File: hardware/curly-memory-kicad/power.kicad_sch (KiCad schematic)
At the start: 19 parts

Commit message: schematic updated with component fields on more components
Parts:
- C? (x5): value C -> 1uF; footprint (none) -> Capacitor_SMD:C_0805_2012Metric_Pad1.18x1.45mm_HandSolder
- C? (x5): value C -> 100nF; footprint (none) -> Capacitor_SMD:C_0805_2012Metric_Pad1.18x1.45mm_HandSolder
- C? (x2): footprint (none) -> Capacitor_SMD:C_0805_2012Metric_Pad1.18x1.45mm_HandSolder
- D? (x2): footprint (none) -> Diode_SMD:D_SMA-SMB_Universal_Handsoldering
- J?: footprint (none) -> Connector_IDC:IDC-Header_2x05_P2.54mm_Vertical
- R? (x2): footprint (none) -> Resistor_SMD:R_0805_2012Metric_Pad1.20x1.40mm_HandSolder
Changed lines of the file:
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@@
       (effects (font (size 1.27 1.27)) (justify left))
     )
-    (property "Value" "C" (id 1) (at 109.601 94.488 0)
-      (effects (font (size 1.27 1.27)) (justify left))
-    )
-    (property "Footprint" "" (id 2) (at 107.6452 97.155 0)
+    (property "Value" "1uF" (id 1) (at 109.601 94.488 0)
+      (effects (font (size 1.27 1.27)) (justify left))
+    )
+    (property "Footprint" "Capacitor_SMD:C_0805_2012Metric_Pad1.18x1.45mm_HandSolder" (id 2) (at 107.6452 97.155 0)
       (effects (font (size 1.27 1.27)) hide)
     )
@@
       (effects (font (size 1.27 1.27)) (justify left))
     )
-    (property "Footprint" "" (id 2) (at 74.422 142.875 90)
+    (property "Footprint" "Resistor_SMD:R_0805_2012Metric_Pad1.20x1.40mm_HandSolder" (id 2) (at 74.422 142.875 90)
       (effects (font (size 1.27 1.27)) hide)
     )
@@
       (effects (font (size 1.27 1.27)) (justify left))
     )
-    (property "Value" "C" (id 1) (at 118.491 94.488 0)
-      (effects (font (size 1.27 1.27)) (justify left))
-    )
-    (property "Footprint" "" (id 2) (at 116.5352 97.155 0)
+    (property "Value" "100nF" (id 1) (at 118.491 94.488 0)
+      (effects (font (size 1.27 1.27)) (justify left))
+    )
+    (property "Footprint" "Capacitor_SMD:C_0805_2012Metric_Pad1.18x1.45mm_HandSolder" (id 2) (at 116.5352 97.155 0)
       (effects (font (size 1.27 1.27)) hide)
     )
@@
       (effects (font (size 1.27 1.27)) (justify left))
     )
-    (property "Value" "C" (id 1) (at 73.406 47.498 0)
-      (effects (font (size 1.27 1.27)) (justify left))
-    )
-    (property "Footprint" "" (id 2) (at 71.4502 50.165 0)
+    (property "Value" "1uF" (id 1) (at 73.406 47.498 0)
+      (effects (font (size 1.27 1.27)) (justify left))
+    )
+    (property "Footprint" "Capacitor_SMD:C_0805_2012Metric_Pad1.18x1.45mm_HandSolder" (id 2) (at 71.4502 50.165 0)
       (effects (font (size 1.27 1.27)) hide)
     )
@@
     (property "Reference" "J?" (id 0) (at 40.64 35.56 0))
     (property "Value" "Conn_02x05_Odd_Even" (id 1) (at 41.91 33.655 0))
-    (property "Footprint" "" (id 2) (at 41.91 46.355 0)
+    (property "Footprint" "Connector_IDC:IDC-Header_2x05_P2.54mm_Vertical" (id 2) (at 41.91 46.355 0)
       (effects (font (size 1.27 1.27)) hide)
     )
@@
       (effects (font (size 1.27 1.27)) (justify left))
     )
-    (property "Value" "C" (id 1) (at 82.296 47.498 0)
-      (effects (font (size 1.27 1.27)) (justify left))
-    )
-    (property "Footprint" "" (id 2) (at 80.3402 50.165 0)
+    (property "Value" "100nF" (id 1) (at 82.296 47.498 0)
+      (effects (font (size 1.27 1.27)) (justify left))
+    )
+    (property "Footprint" "Capacitor_SMD:C_0805_2012Metric_Pad1.18x1.45mm_HandSolder" (id 2) (at 80.3402 50.165 0)
       (effects (font (size 1.27 1.27)) hide)
     )
@@
       (effects (font (size 1.27 1.27)) (justify left))
     )
-    (property "Value" "C" (id 1) (at 81.661 94.488 0)
-      (effects (font (size 1.27 1.27)) (justify left))
-    )
-    (property "Footprint" "" (id 2) (at 79.7052 97.155 0)
+    (property "Value" "100nF" (id 1) (at 81.661 94.488 0)
+      (effects (font (size 1.27 1.27)) (justify left))
+    )
+    (property "Footprint" "Capacitor_SMD:C_0805_2012Metric_Pad1.18x1.45mm_HandSolder" (id 2) (at 79.7052 97.155 0)
       (effects (font (size 1.27 1.27)) hide)
     )
@@
       (effects (font (size 1.27 1.27)) (justify left))
     )
-    (property "Footprint" "" (id 2) (at 65.7352 141.605 0)
+    (property "Footprint" "Capacitor_SMD:C_0805_2012Metric_Pad1.18x1.45mm_HandSolder" (id 2) (at 65.7352 141.605 0)
       (effects (font (size 1.27 1.27)) hide)
     )
@@
       (effects (font (size 1.27 1.27)) (justify left))
     )
-    (property "Value" "C" (id 1) (at 72.771 94.488 0)
-      (effects (font (size 1.27 1.27)) (justify left))
-    )
-    (property "Footprint" "" (id 2) (at 70.8152 97.155 0)
+    (property "Value" "1uF" (id 1) (at 72.771 94.488 0)
+      (effects (font (size 1.27 1.27)) (justify left))
+    )
+    (property "Footprint" "Capacitor_SMD:C_0805_2012Metric_Pad1.18x1.45mm_HandSolder" (id 2) (at 70.8152 97.155 0)
       (effects (font (size 1.27 1.27)) hide)
     )
@@
     (property "Reference" "D?" (id 0) (at 55.88 35.7632 0))
     (property "Value" "D" (id 1) (at 55.88 38.0746 0))
-    (property "Footprint" "" (id 2) (at 55.88 41.275 0)
+    (property "Footprint" "Diode_SMD:D_SMA-SMB_Universal_Handsoldering" (id 2) (at 55.88 41.275 0)
       (effects (font (size 1.27 1.27)) hide)
     )
@@
       (effects (font (size 1.27 1.27)) (justify left))
     )
-    (property "Value" "C" (id 1) (at 82.296 65.278 0)
-      (effects (font (size 1.27 1.27)) (justify left))
-    )
-    (property "Footprint" "" (id 2) (at 80.3402 67.945 0)
+    (property "Value" "100nF" (id 1) (at 82.296 65.278 0)
+      (effects (font (size 1.27 1.27)) (justify left))
+    )
+    (property "Footprint" "Capacitor_SMD:C_0805_2012Metric_Pad1.18x1.45mm_HandSolder" (id 2) (at 80.3402 67.945 0)
       (effects (font (size 1.27 1.27)) hide)
     )
@@
       (effects (font (size 1.27 1.27)) (justify left))
     )
-    (property "Value" "C" (id 1) (at 73.406 65.278 0)
-      (effects (font (size 1.27 1.27)) (justify left))
-    )
-    (property "Footprint" "" (id 2) (at 71.4502 67.945 0)
+    (property "Value" "1uF" (id 1) (at 73.406 65.278 0)
+      (effects (font (size 1.27 1.27)) (justify left))
+    )
+    (property "Footprint" "Capacitor_SMD:C_0805_2012Metric_Pad1.18x1.45mm_HandSolder" (id 2) (at 71.4502 67.945 0)
       (effects (font (size 1.27 1.27)) hide)
     )
@@
       (effects (font (size 1.27 1.27)) (justify left))
     )
-    (property "Footprint" "" (id 2) (at 88.5952 146.685 0)
+    (property "Footprint" "Capacitor_SMD:C_0805_2012Metric_Pad1.18x1.45mm_HandSolder" (id 2) (at 88.5952 146.685 0)
       (effects (font (size 1.27 1.27)) hide)
     )
@@
       (effects (font (size 1.27 1.27)) (justify left))
     )
-    (property "Value" "C" (id 1) (at 109.601 47.498 0)
-      (effects (font (size 1.27 1.27)) (justify left))
-    )
-    (property "Footprint" "" (id 2) (at 107.6452 50.165 0)
+    (property "Value" "1uF" (id 1) (at 109.601 47.498 0)
+      (effects (font (size 1.27 1.27)) (justify left))
+    )
+    (property "Footprint" "Capacitor_SMD:C_0805_2012Metric_Pad1.18x1.45mm_HandSolder" (id 2) (at 107.6452 50.165 0)
       (effects (font (size 1.27 1.27)) hide)
     )
@@
       (effects (font (size 1.27 1.27)) (justify left))
     )
-    (property "Value" "C" (id 1) (at 118.491 47.498 0)
-      (effects (font (size 1.27 1.27)) (justify left))
-    )
-    (property "Footprint" "" (id 2) (at 116.5352 50.165 0)
+    (property "Value" "100nF" (id 1) (at 118.491 47.498 0)
+      (effects (font (size 1.27 1.27)) (justify left))
+    )
+    (property "Footprint" "Capacitor_SMD:C_0805_2012Metric_Pad1.18x1.45mm_HandSolder" (id 2) (at 116.5352 50.165 0)
       (effects (font (size 1.27 1.27)) hide)
     )
@@
       (effects (font (size 1.27 1.27)) (justify left))
     )
-    (property "Footprint" "" (id 2) (at 74.422 132.715 90)
+    (property "Footprint" "Resistor_SMD:R_0805_2012Metric_Pad1.20x1.40mm_HandSolder" (id 2) (at 74.422 132.715 90)
       (effects (font (size 1.27 1.27)) hide)
     )
@@
     (property "Reference" "D?" (id 0) (at 55.88 64.135 0))
     (property "Value" "D" (id 1) (at 55.88 61.595 0))
-    (property "Footprint" "" (id 2) (at 55.88 59.055 0)
-      (effects (font (size 1.27 1.27)) hide)
-    )
+    (property "Footprint" "Diode_SMD:D_SMA-SMB_Universal_Handsoldering" (id 2) (at 55.88 59.055 0)
+      (effects (font (size 1.27 1.27)) hide)
+    )

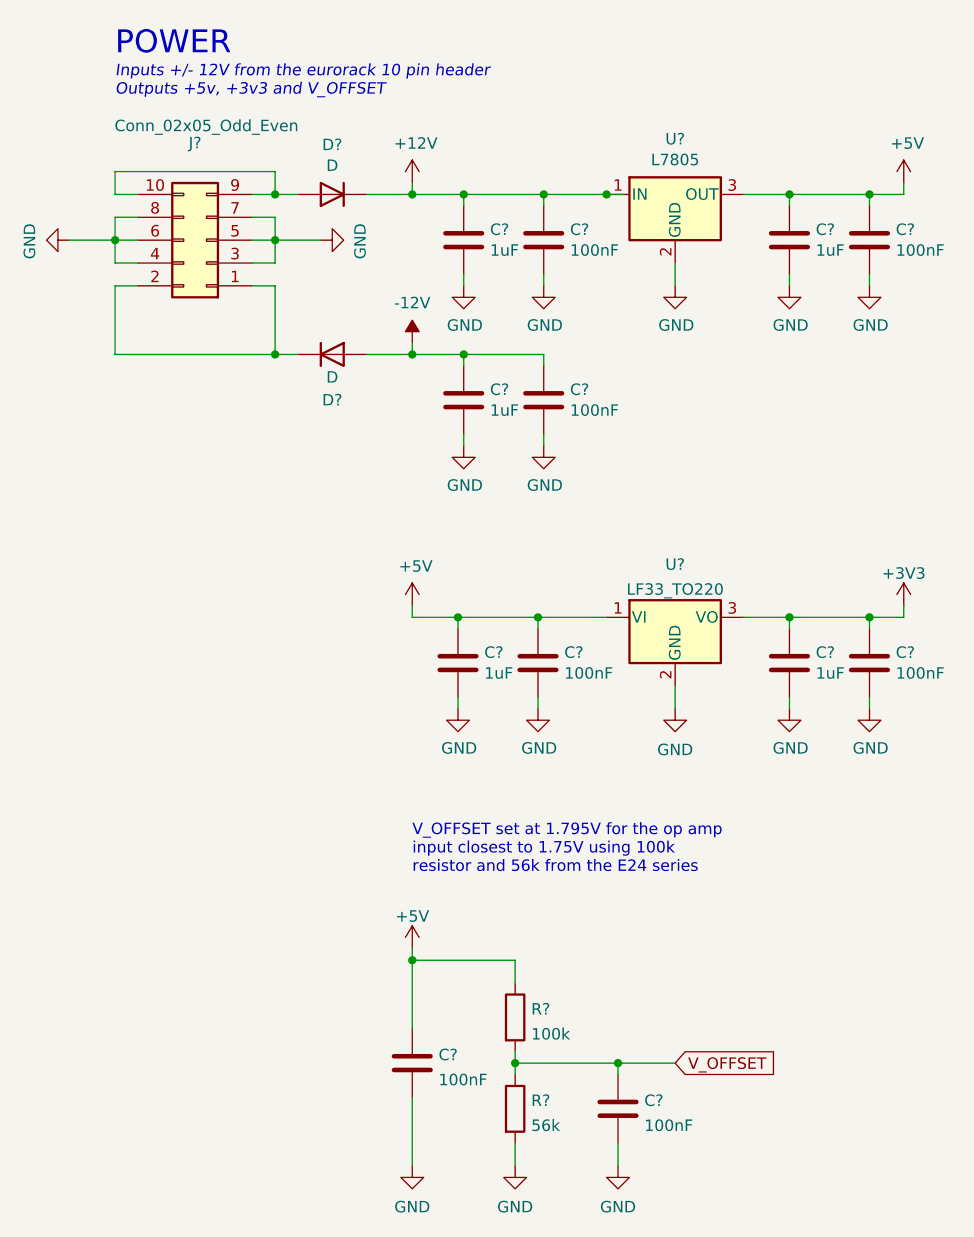
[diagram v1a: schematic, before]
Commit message: all components have part numbers
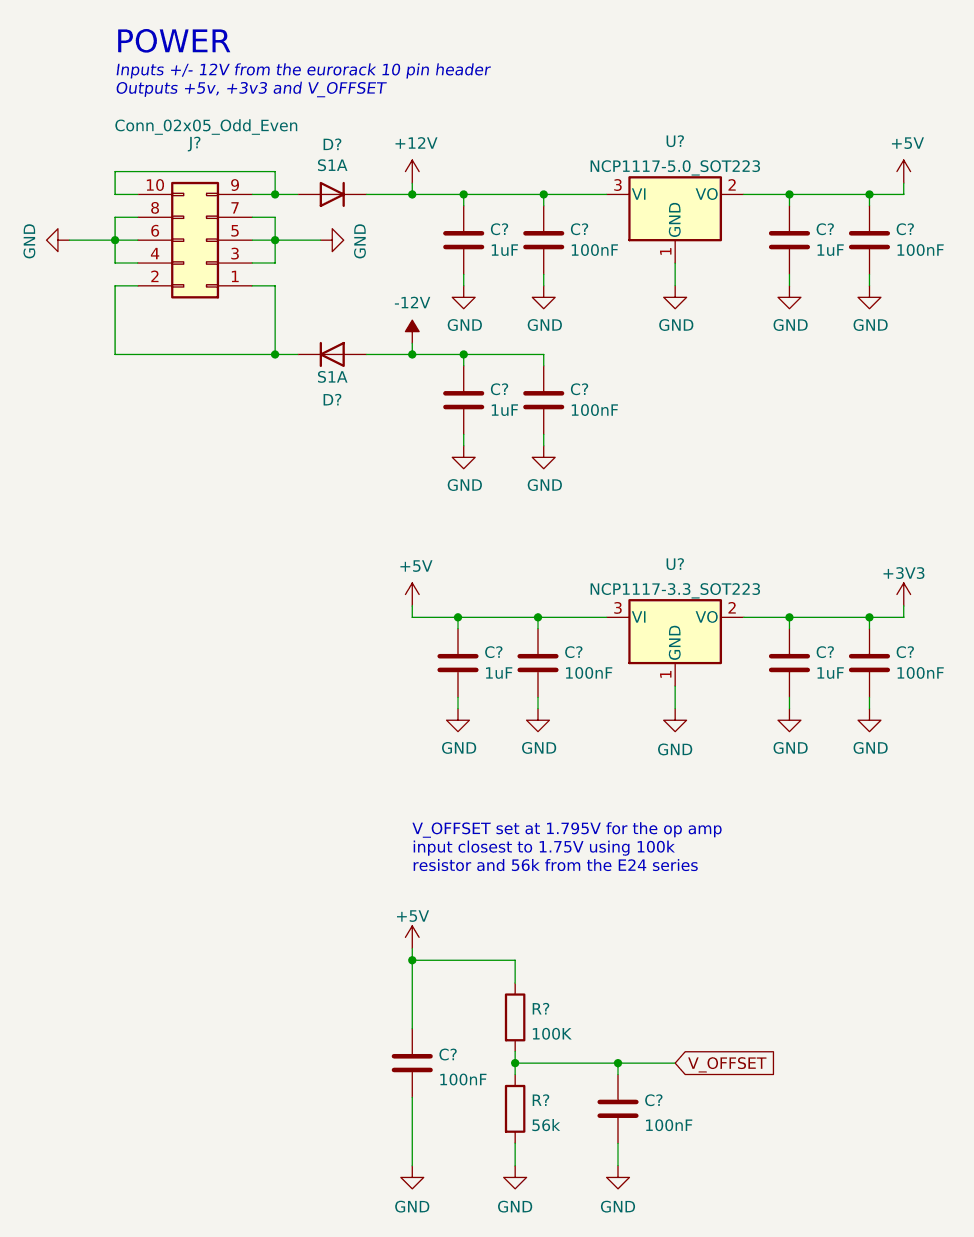
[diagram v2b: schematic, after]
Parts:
- removed U?: L7805, symbol Regulator_Linear:L7805
- removed U?: LF33_TO220, Package_TO_SOT_THT:TO-220-3_Vertical, symbol Regulator_Linear:LF33_TO220
- added U?: NCP1117-5.0_SOT223, Package_TO_SOT_SMD:SOT-223-3_TabPin2, symbol Regulator_Linear:NCP1117-5.0_SOT223
- added U?: NCP1117-3.3_SOT223, Package_TO_SOT_SMD:SOT-223-3_TabPin2, symbol Regulator_Linear:NCP1117-3.3_SOT223
- D? (x2): value D -> S1A
- R?: value 100k -> 100K
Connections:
- net +12V: now also U?.3 (VI)
- net +3V3: now also U?.2 (VO)
- net +5V: now also U?.2 (VO), U?.3 (VI)
- net GND: now also U?.1 (GND), U?.1 (GND)
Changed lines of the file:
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@@
   (junction (at 70.485 59.055) (diameter 0) (color 0 0 0 0)
   )
+  (junction (at 64.77 59.055) (diameter 0) (color 0 0 0 0)
+  )
+  (junction (at 31.75 46.355) (diameter 0) (color 0 0 0 0)
+  )
+  (junction (at 106.68 41.275) (diameter 0) (color 0 0 0 0)
+  )
+  (junction (at 70.485 41.275) (diameter 0) (color 0 0 0 0)
+  )
+  (junction (at 49.53 41.275) (diameter 0) (color 0 0 0 0)
+  )
+  (junction (at 115.57 88.265) (diameter 0) (color 0 0 0 0)
+  )
+  (junction (at 115.57 41.275) (diameter 0) (color 0 0 0 0)
+  )
+  (junction (at 106.68 88.265) (diameter 0) (color 0 0 0 0)
+  )
+  (junction (at 69.85 88.265) (diameter 0) (color 0 0 0 0)
+  )
+  (junction (at 78.74 88.265) (diameter 0) (color 0 0 0 0)
+  )
   (junction (at 79.375 41.275) (diameter 0) (color 0 0 0 0)
   )
-  (junction (at 64.77 59.055) (diameter 0) (color 0 0 0 0)
-  )
-  (junction (at 31.75 46.355) (diameter 0) (color 0 0 0 0)
-  )
-  (junction (at 106.68 41.275) (diameter 0) (color 0 0 0 0)
-  )
-  (junction (at 86.36 41.275) (diameter 0) (color 0 0 0 0)
-  )
-  (junction (at 70.485 41.275) (diameter 0) (color 0 0 0 0)
-  )
-  (junction (at 49.53 41.275) (diameter 0) (color 0 0 0 0)
-  )
-  (junction (at 115.57 88.265) (diameter 0) (color 0 0 0 0)
-  )
-  (junction (at 115.57 41.275) (diameter 0) (color 0 0 0 0)
-  )
-  (junction (at 106.68 88.265) (diameter 0) (color 0 0 0 0)
-  )
-  (junction (at 69.85 88.265) (diameter 0) (color 0 0 0 0)
-  )
-  (junction (at 78.74 88.265) (diameter 0) (color 0 0 0 0)
-  )
   (junction (at 49.53 46.355) (diameter 0) (color 0 0 0 0)
   )
@@
     (stroke (width 0) (type default) (color 0 0 0 0))
   )
-  (wire (pts (xy 86.36 41.275) (xy 88.265 41.275))
-    (stroke (width 0) (type default) (color 0 0 0 0))
-  )
   (wire (pts (xy 64.77 57.785) (xy 64.77 59.055))
     (stroke (width 0) (type default) (color 0 0 0 0))
@@
     (stroke (width 0) (type default) (color 0 0 0 0))
   )
+  (wire (pts (xy 79.375 41.275) (xy 86.36 41.275))
+    (stroke (width 0) (type default) (color 0 0 0 0))
+  )
   (wire (pts (xy 31.75 46.355) (xy 31.75 48.895))
     (stroke (width 0) (type default) (color 0 0 0 0))
   )
   (wire (pts (xy 76.2 136.525) (xy 76.2 137.795))
-    (stroke (width 0) (type default) (color 0 0 0 0))
-  )
-  (wire (pts (xy 79.375 41.275) (xy 86.36 41.275))
     (stroke (width 0) (type default) (color 0 0 0 0))
   )
@@
     (pin "2")
   )
-  (symbol (lib_id "Regulator_Linear:L7805") (at 93.98 41.275 0) (unit 1)
-    (in_bom yes) (on_board yes)
-    (property "Reference" "U?" (id 0) (at 93.98 35.1282 0))
-    (property "Value" "L7805" (id 1) (at 93.98 37.4396 0))
-    (property "Footprint" "" (id 2) (at 94.615 45.085 0)
-      (effects (font (size 1.27 1.27) italic) (justify left) hide)
-    )
-    (property "Datasheet" "http://www.st.com/content/ccc/resource/technical/document/datasheet/41/4f/b3/b0/12/d4/47/88/CD00000444.pdf/files/CD00000444.pdf/jcr:content/translations/en.CD00000444.pdf" (id 3) (at 93.98 42.545 0)
-      (effects (font (size 1.27 1.27)) hide)
-    )
-    (pin "1")
-    (pin "2")
-    (pin "3")
-  )
   (symbol (lib_id "power:+3V3") (at 119.38 86.995 0) (unit 1)
     (in_bom yes) (on_board yes) (fields_autoplaced)
@@
     (pin "1")
   )
-  (symbol (lib_id "Regulator_Linear:LF33_TO220") (at 93.98 88.265 0) (unit 1)
-    (in_bom yes) (on_board yes) (fields_autoplaced)
-    (property "Reference" "U?" (id 0) (at 93.98 82.3935 0))
-    (property "Value" "LF33_TO220" (id 1) (at 93.98 85.1686 0))
-    (property "Footprint" "Package_TO_SOT_THT:TO-220-3_Vertical" (id 2) (at 93.98 82.55 0)
-      (effects (font (size 1.27 1.27) italic) hide)
-    )
-    (property "Datasheet" "http://www.st.com/content/ccc/resource/technical/document/datasheet/c4/0e/7e/2a/be/bc/4c/bd/CD00000546.pdf/files/CD00000546.pdf/jcr:content/translations/en.CD00000546.pdf" (id 3) (at 93.98 89.535 0)
-      (effects (font (size 1.27 1.27)) hide)
-    )
-    (pin "1")
-    (pin "2")
-    (pin "3")
-  )
   (symbol (lib_id "Device:C") (at 78.74 93.345 0) (unit 1)
     (in_bom yes) (on_board yes)
@@
     (pin "1")
   )
+  (symbol (lib_id "Regulator_Linear:NCP1117-5.0_SOT223") (at 93.98 41.275 0) (unit 1)
+    (in_bom yes) (on_board yes) (fields_autoplaced)
+    (property "Reference" "U?" (id 0) (at 93.98 35.4035 0))
+    (property "Value" "NCP1117-5.0_SOT223" (id 1) (at 93.98 38.1786 0))
+    (property "Footprint" "Package_TO_SOT_SMD:SOT-223-3_TabPin2" (id 2) (at 93.98 36.195 0)
+      (effects (font (size 1.27 1.27)) hide)
+    )
+    (property "Datasheet" "http://www.onsemi.com/pub_link/Collateral/NCP1117-D.PDF" (id 3) (at 96.52 47.625 0)
+      (effects (font (size 1.27 1.27)) hide)
+    )
+    (pin "1")
+    (pin "2")
+    (pin "3")
+  )
   (symbol (lib_name "GND_16") (lib_id "power:GND") (at 87.63 149.225 0) (unit 1)
     (in_bom yes) (on_board yes) (fields_autoplaced)
@@
     (in_bom yes) (on_board yes)
     (property "Reference" "D?" (id 0) (at 55.88 35.7632 0))
-    (property "Value" "D" (id 1) (at 55.88 38.0746 0))
+    (property "Value" "S1A" (id 1) (at 55.88 38.0746 0))
     (property "Footprint" "Diode_SMD:D_SMA-SMB_Universal_Handsoldering" (id 2) (at 55.88 41.275 0)
       (effects (font (size 1.27 1.27)) hide)
@@
     (pin "1")
   )
+  (symbol (lib_id "Regulator_Linear:NCP1117-3.3_SOT223") (at 93.98 88.265 0) (unit 1)
+    (in_bom yes) (on_board yes) (fields_autoplaced)
+    (property "Reference" "U?" (id 0) (at 93.98 82.3935 0))
+    (property "Value" "NCP1117-3.3_SOT223" (id 1) (at 93.98 85.1686 0))
+    (property "Footprint" "Package_TO_SOT_SMD:SOT-223-3_TabPin2" (id 2) (at 93.98 83.185 0)
+      (effects (font (size 1.27 1.27)) hide)
+    )
+    (property "Datasheet" "http://www.onsemi.com/pub_link/Collateral/NCP1117-D.PDF" (id 3) (at 96.52 94.615 0)
+      (effects (font (size 1.27 1.27)) hide)
+    )
+    (pin "1")
+    (pin "2")
+    (pin "3")
+  )
   (symbol (lib_id "Device:C") (at 70.485 64.135 0) (unit 1)
     (in_bom yes) (on_board yes)
@@
       (effects (font (size 1.27 1.27)) (justify left))
     )
-    (property "Value" "100k" (id 1) (at 77.978 134.5816 0)
+    (property "Value" "100K" (id 1) (at 77.978 134.5816 0)
       (effects (font (size 1.27 1.27)) (justify left))
     )
@@
     (in_bom yes) (on_board yes)
     (property "Reference" "D?" (id 0) (at 55.88 64.135 0))
-    (property "Value" "D" (id 1) (at 55.88 61.595 0))
+    (property "Value" "S1A" (id 1) (at 55.88 61.595 0))
     (property "Footprint" "Diode_SMD:D_SMA-SMB_Universal_Handsoldering" (id 2) (at 55.88 59.055 0)
       (effects (font (size 1.27 1.27)) hide)
